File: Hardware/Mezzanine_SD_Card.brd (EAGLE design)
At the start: 30.5 x 44.5 mm, 10 parts, among them U2 EDISON_CONNECTOR_FULLMOUNTING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, U3 EDISON_CONNECTOR_FULLHEADER

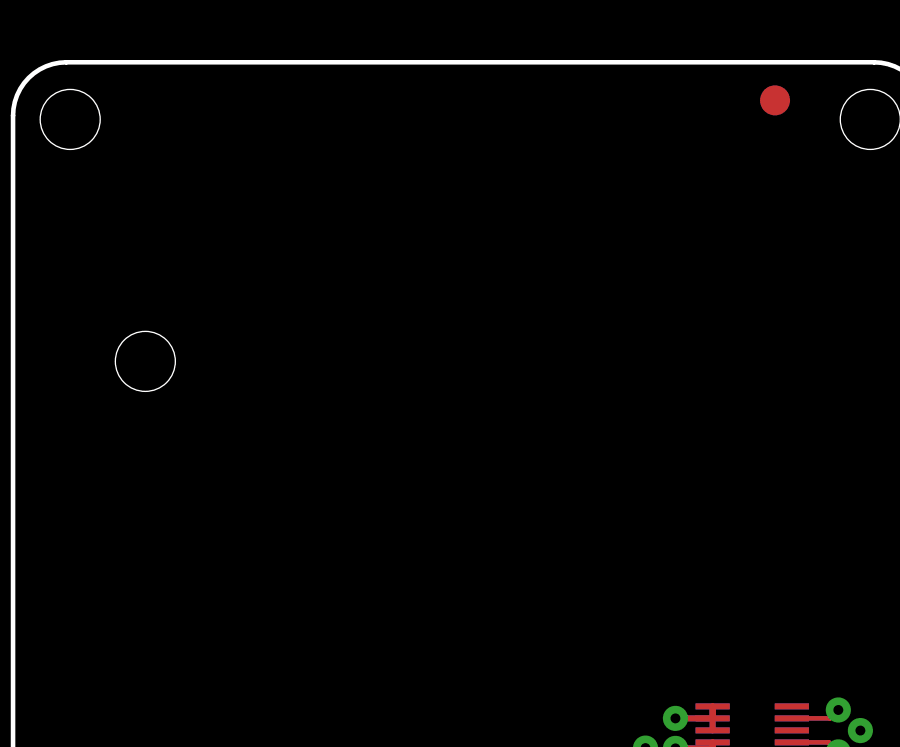
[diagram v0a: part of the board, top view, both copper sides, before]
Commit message: renamed template and added SD, still needs work for level shifting
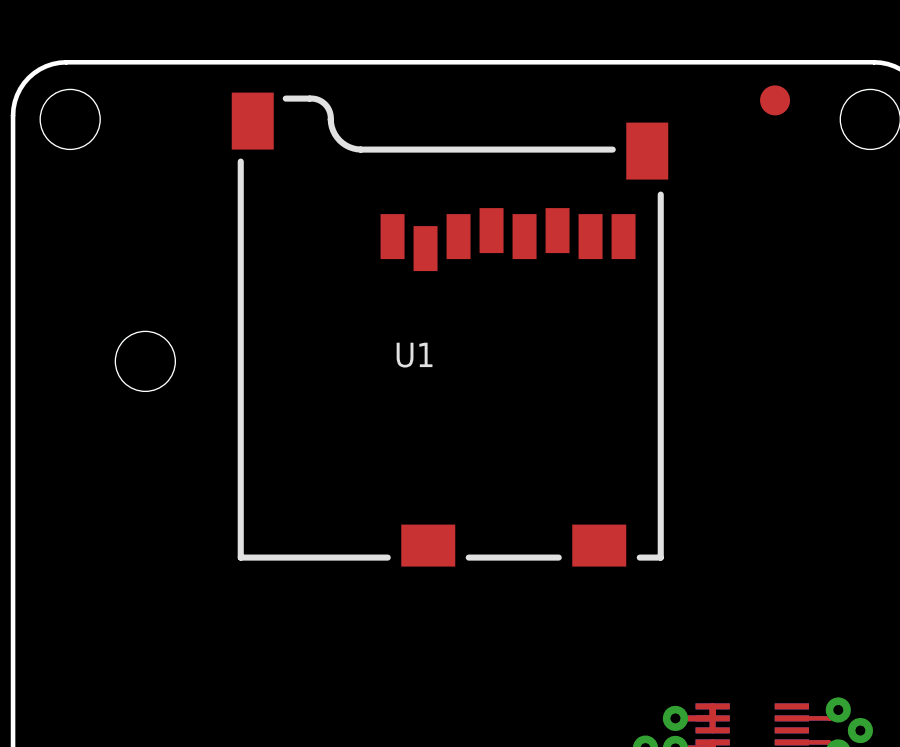
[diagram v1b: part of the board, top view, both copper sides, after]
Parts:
- added U1: USD-SOCKETNEW, SparkFun-Connectors:MICRO-SD-SOCKET-PP
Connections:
- net GND: now also U1.CD1, U1.CD2, U1.GND1, U1.GND3
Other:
- board text added: "Edzzanine SD"
- board text removed: "Example Name of Board"
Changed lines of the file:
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@@
 <setting verticaltext="up"/>
 </settings>
-<grid distance="0.05" unitdist="inch" unit="inch" style="lines" multiple="1" display="yes" altdistance="0.005" altunitdist="inch" altunit="inch"/>
+<grid distance="0.4" unitdist="mm" unit="mm" style="lines" multiple="1" display="yes" altdistance="0.005" altunitdist="inch" altunit="inch"/>
 <layers>
 <layer number="1" name="Top" color="4" fill="1" visible="yes" active="yes"/>
@@
 <text x="-2.54" y="41.91" size="1.778" layer="51" rot="R270">LED's and selector switches go here</text>
 <text x="31.115" y="39.37" size="1.778" layer="51" rot="R270">Nothing goes here...  I mean it.</text>
-<text x="29.337" y="29.21" size="1.27" layer="22" font="vector" ratio="15" rot="MR90" align="center">Example Name of Board</text>
+<text x="29.337" y="29.21" size="1.27" layer="22" font="vector" ratio="15" rot="MR90" align="center">Edzzanine SD</text>
 <wire x1="1.778" y1="44.45" x2="28.702" y2="44.45" width="0.1524" layer="20"/>
 <wire x1="30.48" y1="44.704" x2="30.48" y2="53.34" width="0.254" layer="51"/>
@@
 <element name="FID1" library="SparkFun-Aesthetics" package="FIDUCIAL-1X2" value="FIDUCIAL1X2" x="1.27" y="5.08"/>
 <element name="FID2" library="SparkFun-Aesthetics" package="FIDUCIAL-1X2" value="FIDUCIAL1X2" x="25.4" y="43.18"/>
+<element name="U1" library="SparkFun-Connectors" package="MICRO-SD-SOCKET-PP" value="USD-SOCKETNEW" x="21.59" y="27.94"/>
 </elements>
 <signals>
@@
 <contactref element="U3" pad="11"/>
 <contactref element="U3" pad="13"/>
+<contactref element="U1" pad="GND3"/>
+<contactref element="U1" pad="CD2"/>
+<contactref element="U1" pad="GND1"/>
+<contactref element="U1" pad="CD1"/>
 </signal>
 <signal name="VSYS">
